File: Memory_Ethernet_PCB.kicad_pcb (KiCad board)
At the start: 2 copper layers, 99.5 x 52 mm, 55 parts, among them J1 WR-BHD_Conn_02x07_Odd_Even, J2 USB_A_Wurth_614004135023, J3 RJ45_Wuerth_74980104400, U1 Infineon S25FL128LAGMFM010, U2 Infineon S25FL128LAGMFM010, U3 USBLC6-2SC6, U4 SIT5000 (25MHz TCXO), U5 W5500

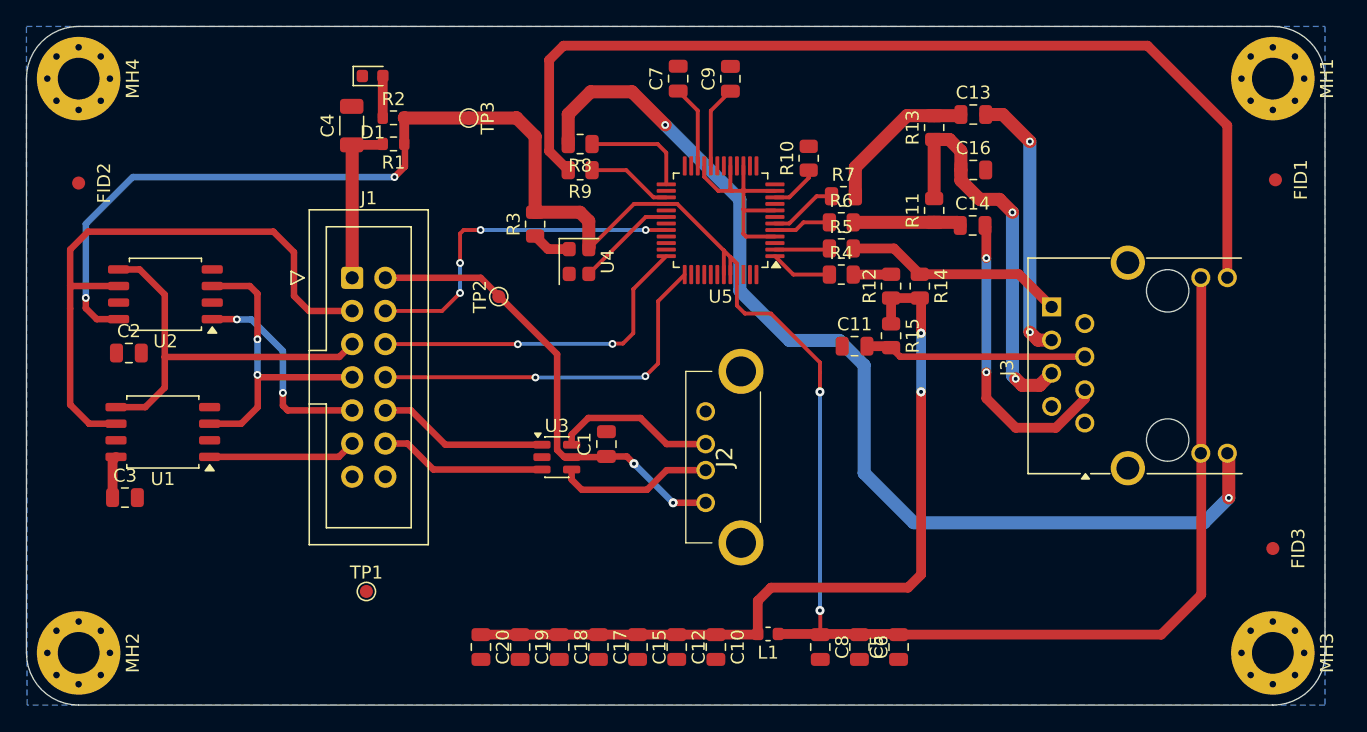
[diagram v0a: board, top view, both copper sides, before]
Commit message: Remove pcb routing
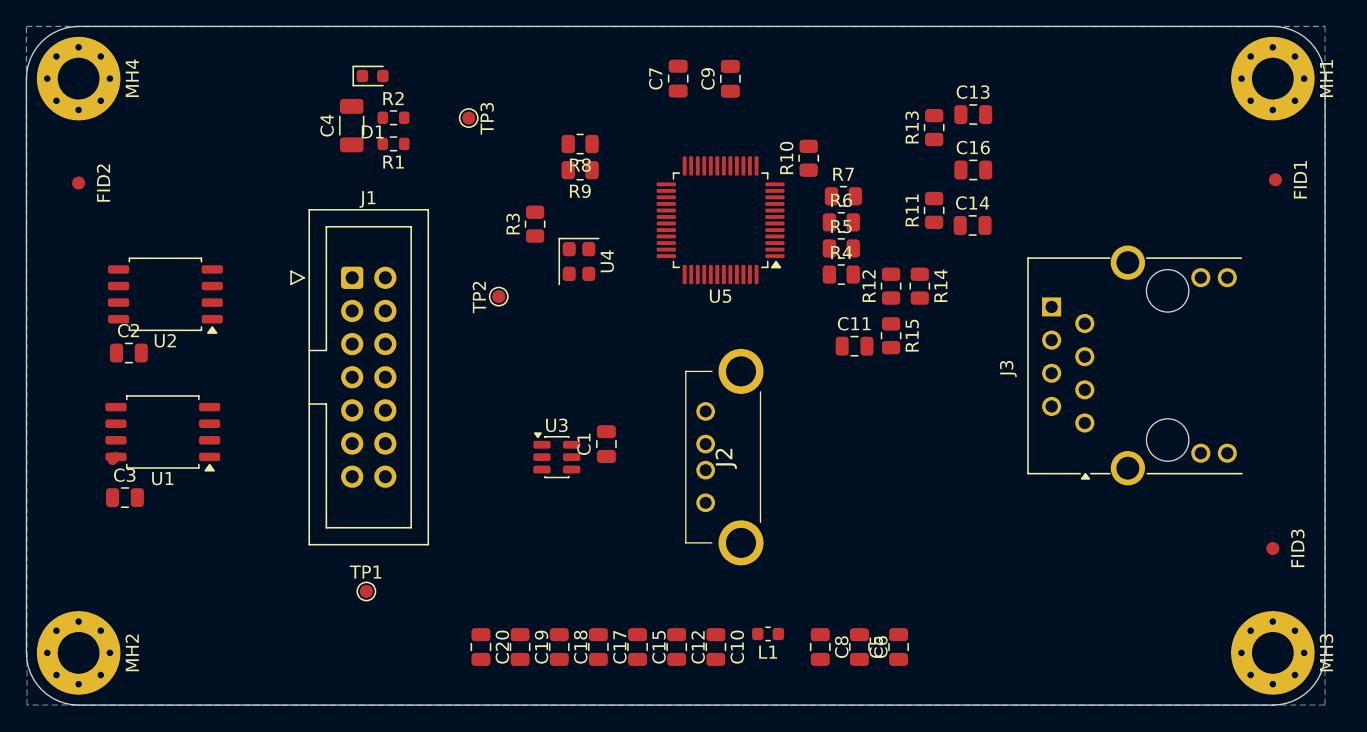
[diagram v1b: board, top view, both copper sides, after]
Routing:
- net +3V3: track 173.7 -> 0.37 mm, vias 4 -> 0
- net +3V3A: track 81.5 -> 0.00 mm, vias 2 -> 0
- net Net-(J3-Pad12): track 80.5 -> 0.16 mm, vias 2 -> 0
- net Net-(J3-Pad10): track 75.7 -> 0.00 mm
- net /SCK_SPI: track 46.4 -> 0.00 mm
- net /5V_VIN: track 36.1 -> 0.00 mm, vias 2 -> 0
- net /MOSI_SPI: track 30.6 -> 0.00 mm
- net /ETH_CRD: track 30.4 -> 0.00 mm, vias 2 -> 0
- net /ETH_RST: track 29.0 -> 0.00 mm, vias 2 -> 0
- net /ETH_CS: track 26.8 -> 0.00 mm, vias 4 -> 0
- net /ETH_INT: track 26.3 -> 0.00 mm, vias 2 -> 0
- net /USB_D+: track 25.6 -> 0.00 mm
- net /USB_D-: track 25.5 -> 0.00 mm
- net /MISO_SPI: track 24.0 -> 0.00 mm, vias 2 -> 0
- net /ETH_RD-: track 23.4 -> 0.00 mm, vias 2 -> 0
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
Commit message: Initial component routing
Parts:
- moved J1 67.1 mm to (178.4, 84.4)
- moved U1 60.9 mm to (156.8, 86.6)
- moved U2 60.7 mm to (156.8, 96.6)
- moved TP2 60.0 mm to (178.7, 108.0), turned to 180 degrees
- moved C3 59.3 mm to (152.2, 91.4), turned to 180 degrees
- moved C2 59.0 mm to (152.3, 101.4), turned to 180 degrees
- moved J3 55.5 mm to (109.4, 85.0), turned to -90 degrees
- moved C4 52.2 mm to (163.3, 77.1), turned to 180 degrees
- moved C16 50.6 mm to (111.9, 95.7), turned to -90 degrees
- moved R1 49.9 mm to (164.2, 79.4), turned to 0 degrees
- moved C13 49.8 mm to (115.4, 96.9), turned to -90 degrees
- moved R13 46.0 mm to (114.7, 94.1), turned to 0 degrees
- moved C14 44.2 mm to (115.3, 89.2), turned to 90 degrees
- moved R11 42.9 mm to (114.7, 92.0), turned to 180 degrees
- moved R2 42.4 mm to (156.9, 72.5)
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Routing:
- net +3V3: track 0.37 -> 150.2 mm, vias 0 -> 3
- net /5V_VIN: track 0.00 -> 80.7 mm
- net +3V3A: track 0.00 -> 77.9 mm, vias 0 -> 2
- net Net-(J3-Pad12): track 0.16 -> 76.1 mm, vias 0 -> 2
- net /MISO_SPI: track 0.00 -> 71.1 mm, vias 0 -> 2
- net /ETH_RST: track 0.00 -> 59.9 mm, vias 0 -> 1
- net /SCK_SPI: track 0.00 -> 58.5 mm, vias 0 -> 3
- net /MOSI_SPI: track 0.00 -> 57.4 mm
- net /ETH_CS: track 0.00 -> 55.2 mm, vias 0 -> 1
- net Net-(J3-Pad10): track 0.00 -> 54.1 mm
- net /ETH_INT: track 0.00 -> 53.7 mm
- net GND: track 0.00 -> 48.9 mm, vias 0 -> 30
- net /USB_D-: track 0.00 -> 43.0 mm
- net /USB_D+: track 0.00 -> 38.1 mm
- net /ETH_TD-: track 0.04 -> 37.9 mm, vias 0 -> 2
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
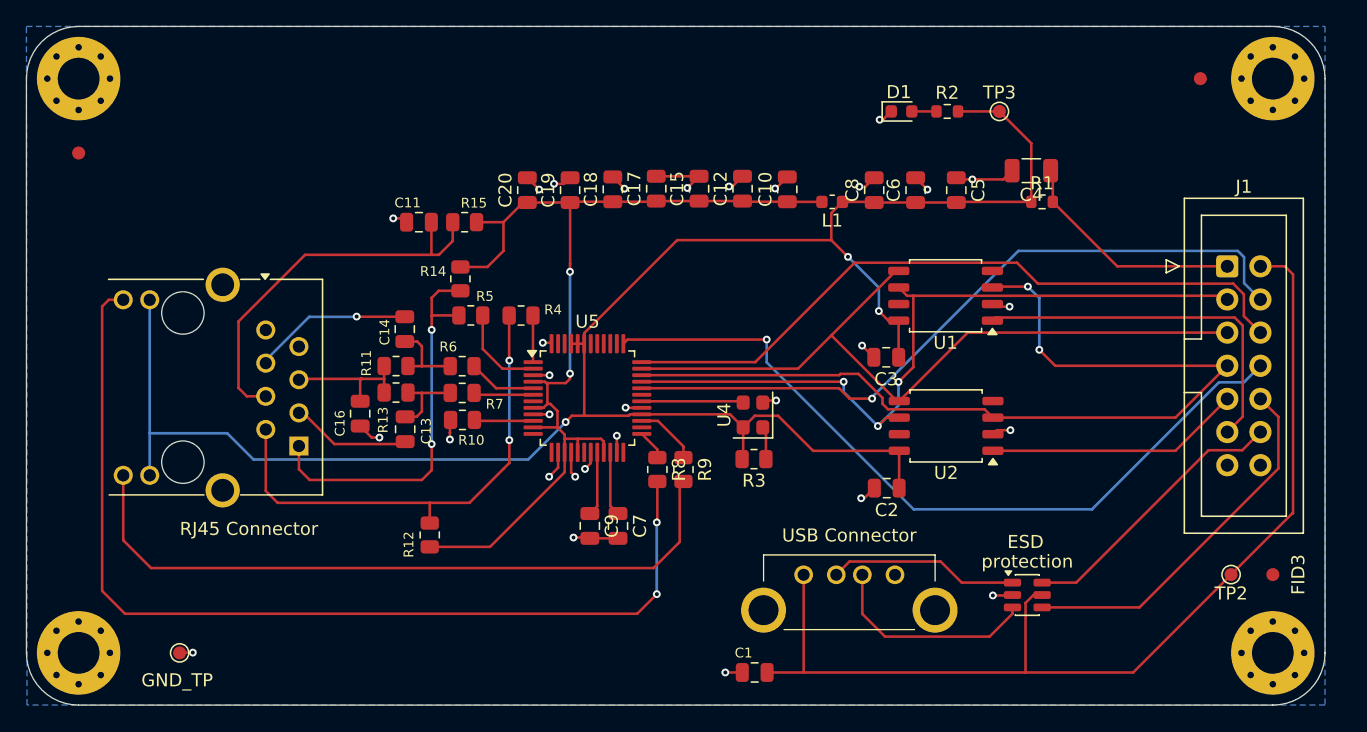
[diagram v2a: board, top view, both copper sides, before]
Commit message: SPI and ETH Routing
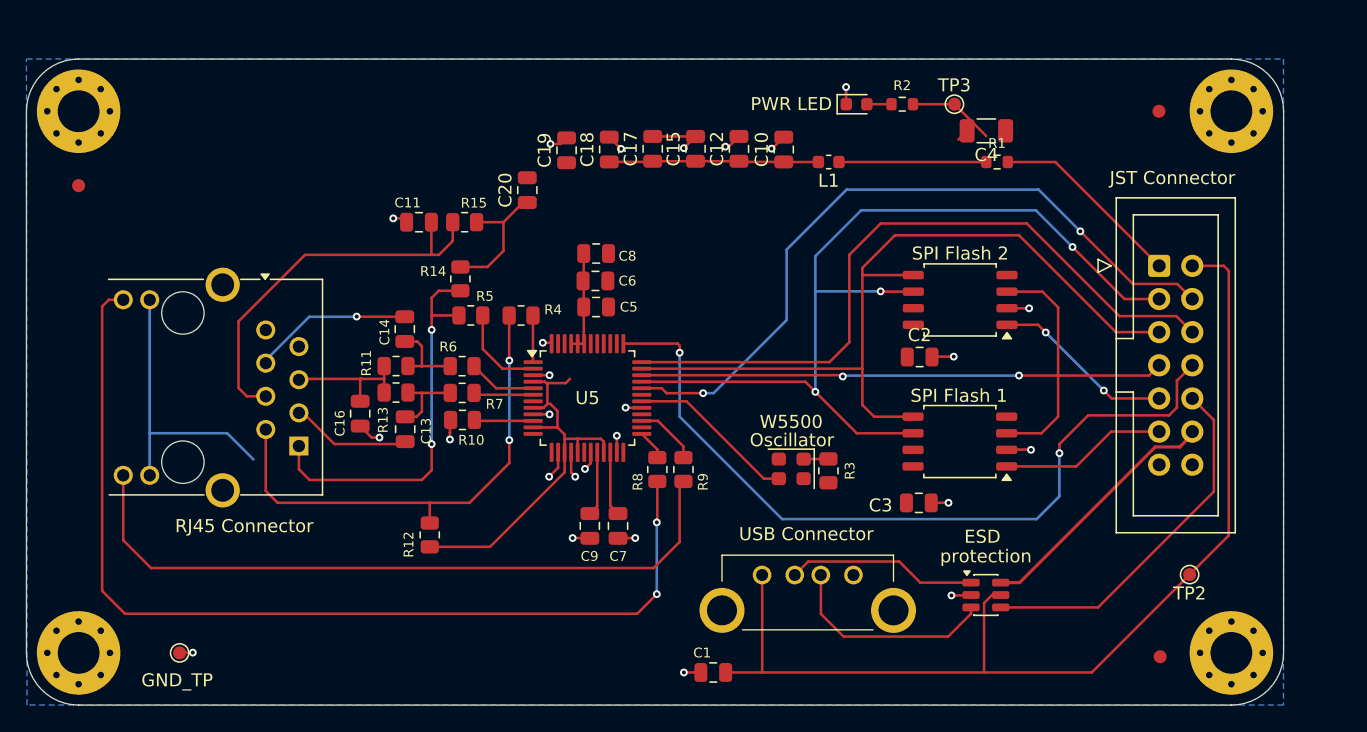
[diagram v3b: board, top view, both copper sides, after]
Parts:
- R3: value ~ -> 4k7
- moved C5 29.0 mm to (130.0, 87.5), turned to 180 degrees
- moved C6 25.5 mm to (129.9, 85.5), turned to 0 degrees
- moved C8 21.9 mm to (130.0, 83.4), turned to 0 degrees
- moved C3 11.4 mm to (154.7, 102.5), turned to 0 degrees
- moved U1 11.2 mm to (157.9, 97.8)
- moved FID3 10.7 mm to (173.2, 114.3)
- moved C2 10.4 mm to (154.8, 91.3), turned to 0 degrees
- moved U2 9.71 mm to (157.9, 87.0)
- moved R3 5.77 mm to (147.8, 100.0), turned to -90 degrees
- moved J1 5.22 mm to (173.1, 84.3)
- moved U4 5.06 mm to (144.9, 99.9), turned to 180 degrees
- moved C4 4.60 mm to (159.9, 74.0)
- moved R1 4.60 mm to (160.7, 76.4)
- moved FID1 4.04 mm to (173.1, 72.5)
- moved MH1 4.04 mm to (178.7, 72.5)
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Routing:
- net +3V3: track 150.2 -> 48.2 mm, vias 3 -> 0
- net +3V3A: track 77.9 -> 57.5 mm, vias 2 -> 0
- net /FLASH1_CS: track 28.2 -> 12.8 mm
- net /MISO_SPI: track 71.1 -> 57.5 mm
- net /SCK_SPI: track 58.5 -> 70.9 mm
- net GND: track 48.9 -> 40.6 mm, vias 30 -> 26
- net /FLASH2_CS: track 19.6 -> 14.0 mm, vias 0 -> 2
- net Net-(U4-CLK/OUT): track 7.81 -> 13.0 mm
- net /MOSI_SPI: track 57.4 -> 62.4 mm
- net /3V3_VIN: track 17.9 -> 14.9 mm
- net /USB_D+: track 38.1 -> 36.0 mm
- net /ETH_RST: track 59.9 -> 60.8 mm, vias 1 -> 2
- net /ETH_CS: track 55.2 -> 55.8 mm, vias 1 -> 2
- net Net-(U4-NC): track 2.53 -> 1.91 mm
- net /USB_D-: track 43.0 -> 42.5 mm
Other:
- board size 99.5 x 52 mm -> 96.3 x 49.5 mm

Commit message: +3V3 Routing
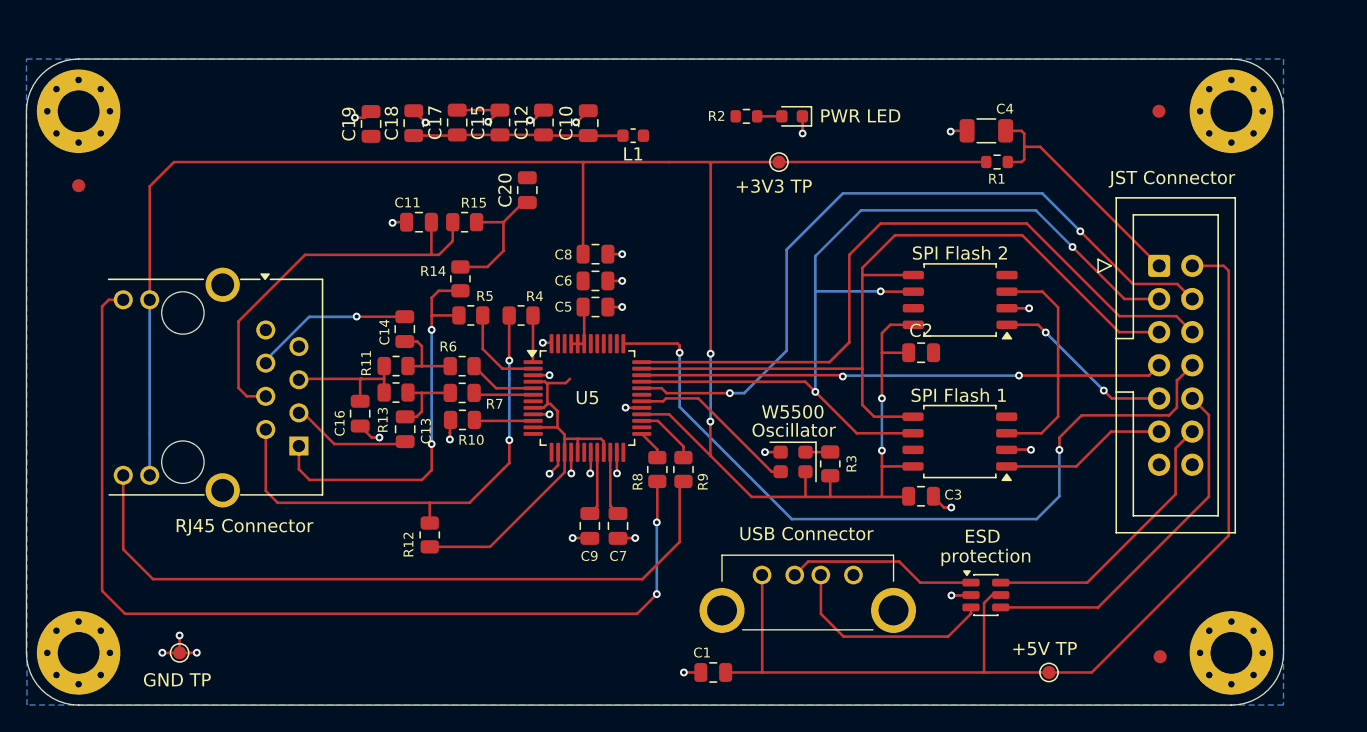
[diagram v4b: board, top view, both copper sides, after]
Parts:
- moved C15 15.1 mm to (122.6, 73.4)
- moved C17 15.1 mm to (119.4, 73.4)
- moved C10 15.1 mm to (129.4, 73.4)
- moved C18 15.1 mm to (116.0, 73.4)
- moved C12 15.1 mm to (126.0, 73.4)
- moved C19 15.1 mm to (112.8, 73.5)
- moved L1 15.1 mm to (132.8, 74.4)
- moved TP3 14.2 mm to (144.0, 76.4)
- moved TP2 13.1 mm to (164.7, 115.5)
- moved R2 12.0 mm to (141.5, 72.9), turned to 180 degrees
- moved D1 5.02 mm to (145.0, 72.9), turned to 180 degrees
- moved U4 0.55 mm to (145.1, 99.4)
- moved R3 0.55 mm to (147.9, 99.5)
- moved C3 0.53 mm to (154.9, 102.0)
- moved C2 0.35 mm to (154.9, 91.0)
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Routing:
- net +3V3: track 48.2 -> 166.9 mm, vias 0 -> 4
- net GND: track 40.6 -> 47.0 mm, vias 26 -> 32
- net /3V3_VIN: track 14.9 -> 19.0 mm
- net /USB_D+: track 36.0 -> 38.0 mm
- net /ETH_CS: track 55.8 -> 57.0 mm
- net Net-(J3-Pad10): track 54.1 -> 55.2 mm
